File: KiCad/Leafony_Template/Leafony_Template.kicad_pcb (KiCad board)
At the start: 4 copper layers, 20 x 20 mm, 1 part, among them CN1 LeafIF

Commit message: Add files via upload
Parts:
- CN1: value LeafIF -> Leafony bus
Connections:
- net /SCK renamed /SCL
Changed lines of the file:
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@@
-(kicad_pcb (version 20171130) (host pcbnew "(5.1.2)-2")
+(kicad_pcb (version 20171130) (host pcbnew "(5.1.5)-3")
   (general
     (thickness 0.8)
@@
   (net 24 /D13)
   (net 25 /SDA)
-  (net 26 /SCK)
-  (net 27 /SWCLK)
-  (net 28 GND)
-  (net 29 +3V3)
+  (net 26 /SWCLK)
+  (net 27 GND)
+  (net 28 +3V3)
+  (net 29 /SCL)
   (net_class Default "This is the default net class."
     (clearance 0.127)
@@
     (add_net /D9)
     (add_net /RESET)
-    (add_net /SCK)
+    (add_net /SCL)
     (add_net /SDA)
     (add_net /SWCLK)
@@
       (effects (font (size 1 1) (thickness 0.15)))
     )
-    (fp_text value LeafIF (at 0 1.625) (layer F.Fab)
+    (fp_text value "Leafony bus" (at 0 1.625) (layer F.Fab) hide
       (effects (font (size 1 1) (thickness 0.15)))
     )
     (pad F27 smd rect (at 12.15 0) (size 0.9 1.45) (layers F.Cu F.Mask)
-      (net 28 GND))
+      (net 27 GND))
     (pad F1 smd rect (at 0 0) (size 0.9 1.45) (layers F.Cu F.Mask)
-      (net 29 +3V3))
+      (net 28 +3V3))
     (pad "" thru_hole circle (at -2.175 -0.975) (size 2.05 2.05) (drill 2.05) (layers *.Cu *.Mask)
       (solder_mask_margin 0.27))
@@
       ))
     (pad F29 smd custom (at 12.375 -1.8) (size 0.45 1.15) (layers F.Cu F.Mask)
-      (net 27 /SWCLK) (zone_connect 0)
+      (net 26 /SWCLK) (zone_connect 0)
       (options (clearance outline) (anchor rect))
       (primitives
@@
       ))
     (pad F25 smd custom (at 11.025 -0.15 180) (size 0.45 1.15) (layers F.Cu F.Mask)
-      (net 26 /SCK) (zone_connect 0)
+      (net 29 /SCL) (zone_connect 0)
       (options (clearance outline) (anchor rect))
       (primitives
@@
       ))
     (pad B27 smd rect (at 12.15 0) (size 0.9 1.45) (layers B.Cu B.Mask)
-      (net 28 GND))
+      (net 27 GND))
     (pad B25 smd custom (at 11.025 -0.15 180) (size 0.45 1.15) (layers B.Cu B.Mask)
-      (net 26 /SCK) (zone_connect 0)
+      (net 29 /SCL) (zone_connect 0)
       (options (clearance outline) (anchor rect))
       (primitives
@@
       ))
     (pad B29 smd custom (at 12.375 -1.8) (size 0.45 1.15) (layers B.Cu B.Mask)
-      (net 27 /SWCLK) (zone_connect 0)
+      (net 26 /SWCLK) (zone_connect 0)
       (options (clearance outline) (anchor rect))
       (primitives
@@
       ))
     (pad B1 smd rect (at 0 0) (size 0.9 1.45) (layers B.Cu B.Mask)
-      (net 29 +3V3))
+      (net 28 +3V3))
   )
   (gr_poly (pts (xy 45 30) (xy 44.5 30) (xy 44.5 45) (xy 45 45)) (layer F.SilkS) (width 0.1))
@@
   (via (at 38.15 28.9) (size 0.5) (drill 0.3) (layers F.Cu B.Cu) (net 24))
   (via (at 39.05 28.9) (size 0.5) (drill 0.3) (layers F.Cu B.Cu) (net 25))
-  (via (at 39.95 28.9) (size 0.5) (drill 0.3) (layers F.Cu B.Cu) (net 26))
-  (via (at 41.3 26.1) (size 0.5) (drill 0.3) (layers F.Cu B.Cu) (net 27))
-  (via (at 40.9 28.9) (size 0.5) (drill 0.3) (layers F.Cu B.Cu) (net 28))
-  (via (at 29.1 28.9) (size 0.5) (drill 0.3) (layers F.Cu B.Cu) (net 29))
+  (via (at 41.3 26.1) (size 0.5) (drill 0.3) (layers F.Cu B.Cu) (net 26))
+  (via (at 40.9 28.9) (size 0.5) (drill 0.3) (layers F.Cu B.Cu) (net 27))
+  (via (at 29.1 28.9) (size 0.5) (drill 0.3) (layers F.Cu B.Cu) (net 28))
+  (via (at 39.95 28.9) (size 0.5) (drill 0.3) (layers F.Cu B.Cu) (net 29))
   (zone (net 0) (net_name "") (layers F.Cu In1.Cu In2.Cu B.Cu) (hatch full 0.508)
     (connect_pads (clearance 0.508))

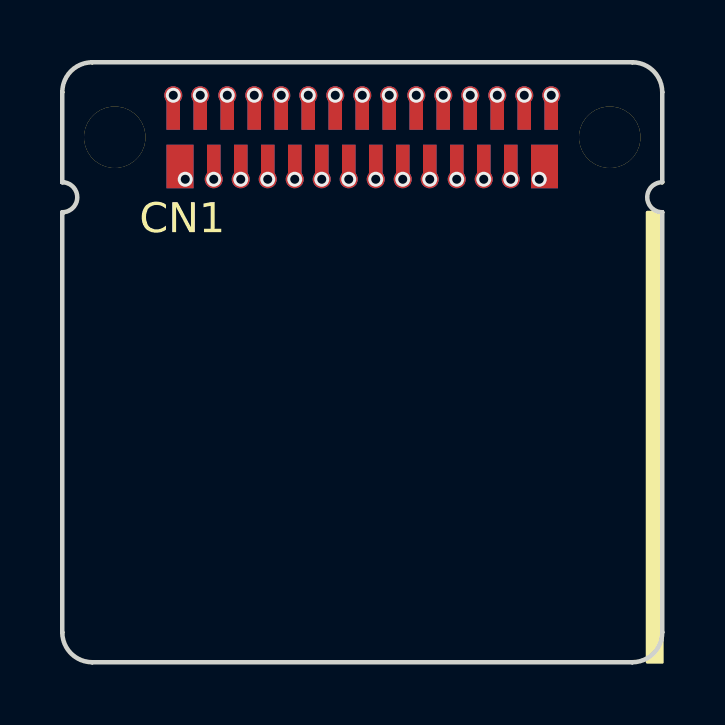
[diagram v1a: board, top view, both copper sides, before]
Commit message: fix DRC errors of kicad template
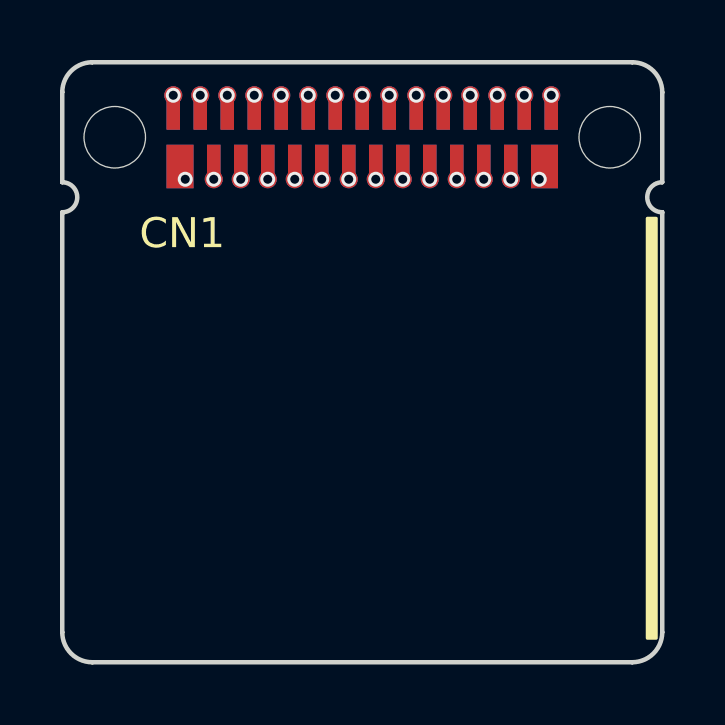
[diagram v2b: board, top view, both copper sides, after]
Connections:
- net +3V3 renamed +3.3V
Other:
- net class Default removed
